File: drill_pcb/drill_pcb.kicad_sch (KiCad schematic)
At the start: 2 parts

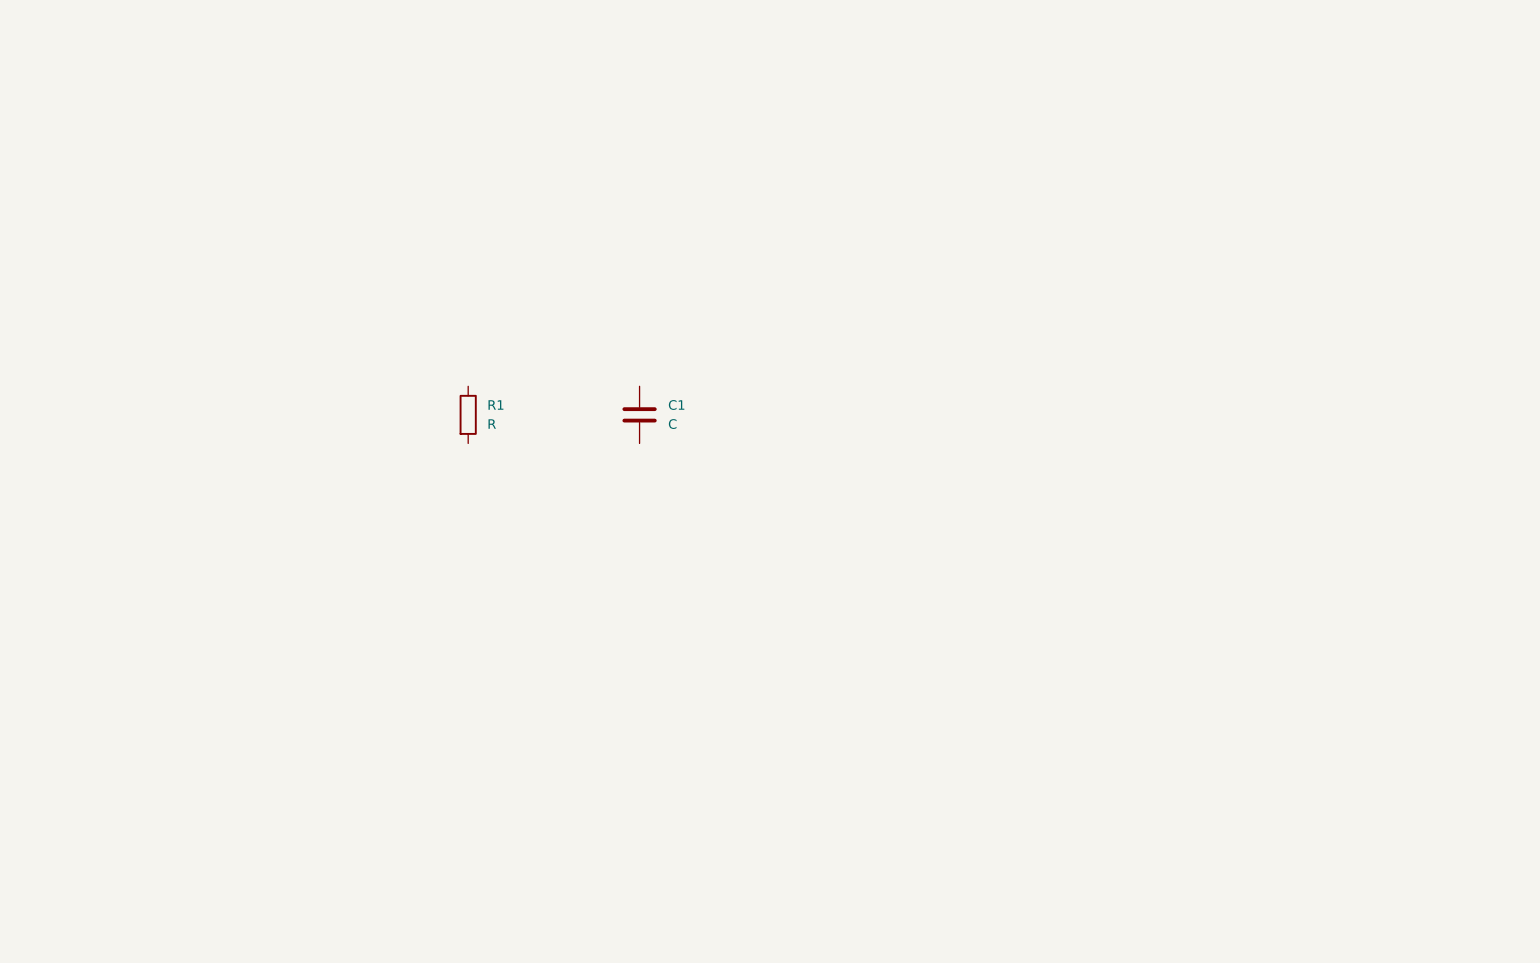
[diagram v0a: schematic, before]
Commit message: fix ERC errors
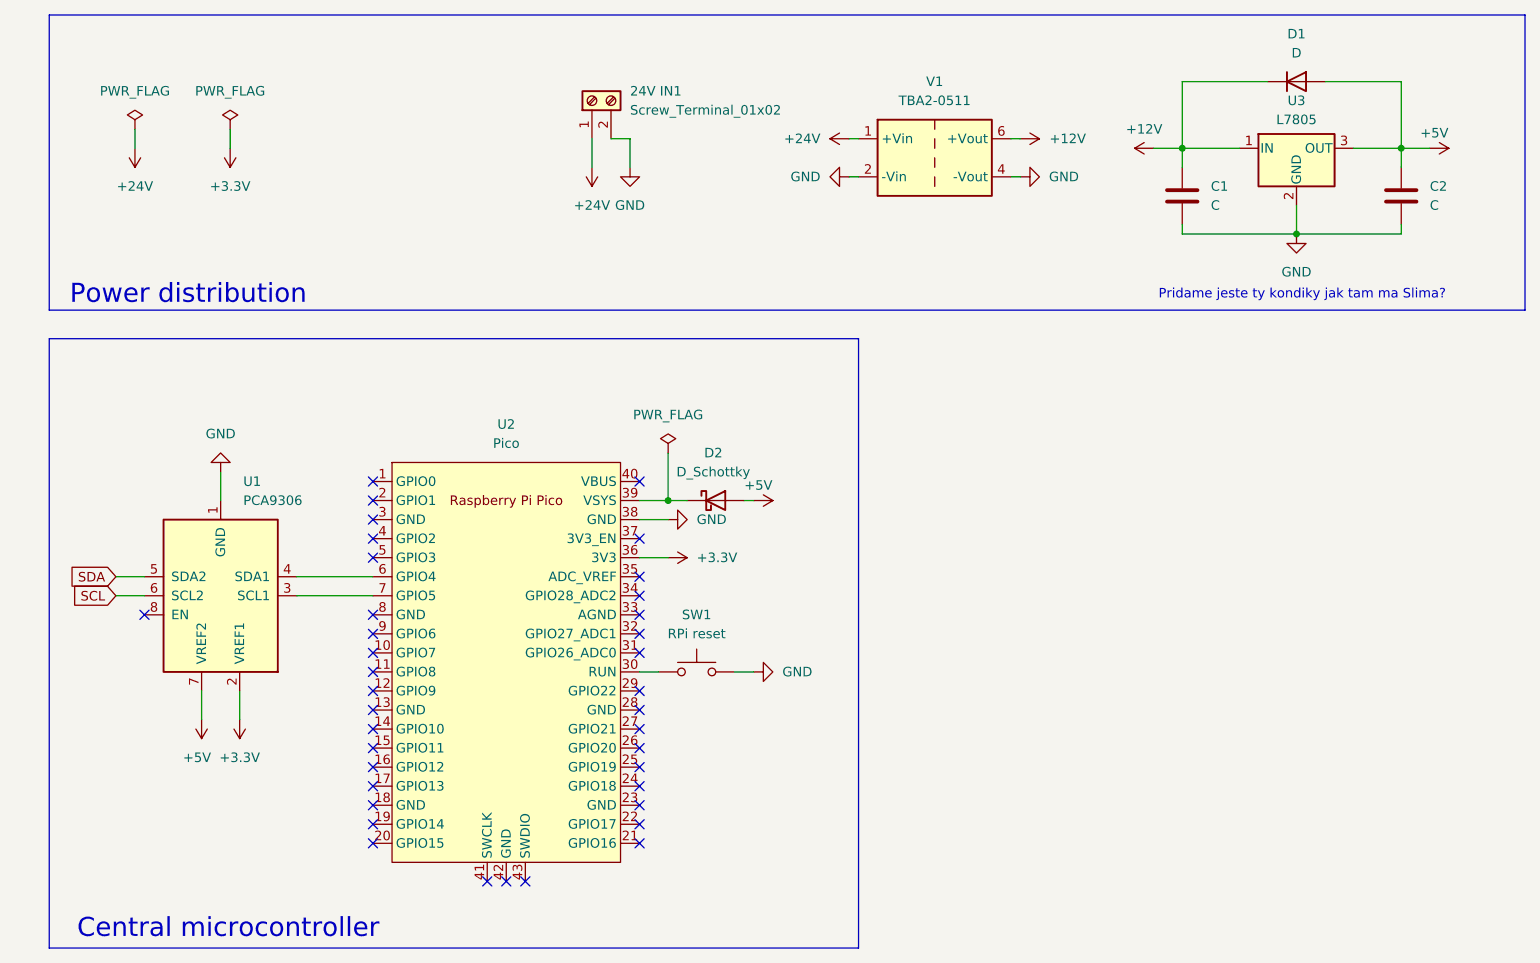
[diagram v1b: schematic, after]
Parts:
- removed R1: R, symbol Device:R
- added 24V IN1: Screw_Terminal_01x02, Connectors:DEANS, symbol Connector:Screw_Terminal_01x02
- added C2: C, Capacitor_SMD:C_1206_3216Metric_Pad1.33x1.80mm_HandSolder, symbol Device:C
- added D1: D, Diode_THT:D_DO-41_SOD81_P7.62mm_Horizontal, symbol Device:D
- added D2: D_Schottky, Diode_SMD:D_SOD-123, symbol Device:D_Schottky
- added SW1: RPi reset, Button_Switch_THT:SW_PUSH_6mm_H5mm, symbol Switch:SW_Push
- added U1: PCA9306, i2c_levl:i2c_levl_shifter, symbol Interface:PCA9306
- added U2: Pico, MCU_RaspberryPi_and_Boards:RPi_Pico_SMD_TH, symbol MCU_RaspberryPi_and_Boards:Pico
- added U3: L7805, Package_TO_SOT_THT:TO-220-3_Vertical, symbol Regulator_Linear:L7805
- added V1: TBA2-0511, i2c_levl:dcdc_menic, symbol Converter_DCDC:TBA2-0511
- C1: footprint (none) -> Capacitor_SMD:C_1206_3216Metric_Pad1.33x1.80mm_HandSolder
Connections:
- net +12V: now reaches C1.1
- net +12V: now also D1.1 (K), U3.1 (IN), V1.6 (+Vout)
- net GND: now reaches C1.2
- net GND: now also 24V IN1.2 (Pin_2), C2.2, SW1.2, U1.1 (GND), U2.38 (GND), U3.2 (GND), V1.2 (-Vin), V1.4 (-Vout)
- new net: D2.1 (K), U2.39 (VSYS)
- new net: SW1.1, U2.30 (RUN)
- new net: U1.4 (SDA1), U2.6 (GPIO4)
- new net: U1.3 (SCL1), U2.7 (GPIO5)
- new net +24V: 24V IN1.1 (Pin_1), V1.1 (+Vin)
- new net +3.3V: U1.2 (VREF1), U2.36 (3V3)
- new net +5V: C2.1, D1.2 (A), D2.2 (A), U1.7 (VREF2), U3.3 (OUT)
- new net SCL: U1.6 (SCL2)
- new net SDA: U1.5 (SDA2)
- no-connect marks 0 -> 38
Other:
- note added: "Central microcontroller"
- note added: "Power distribution"
- note added: "Pridame jeste ty kondiky jak tam ma Slima?"

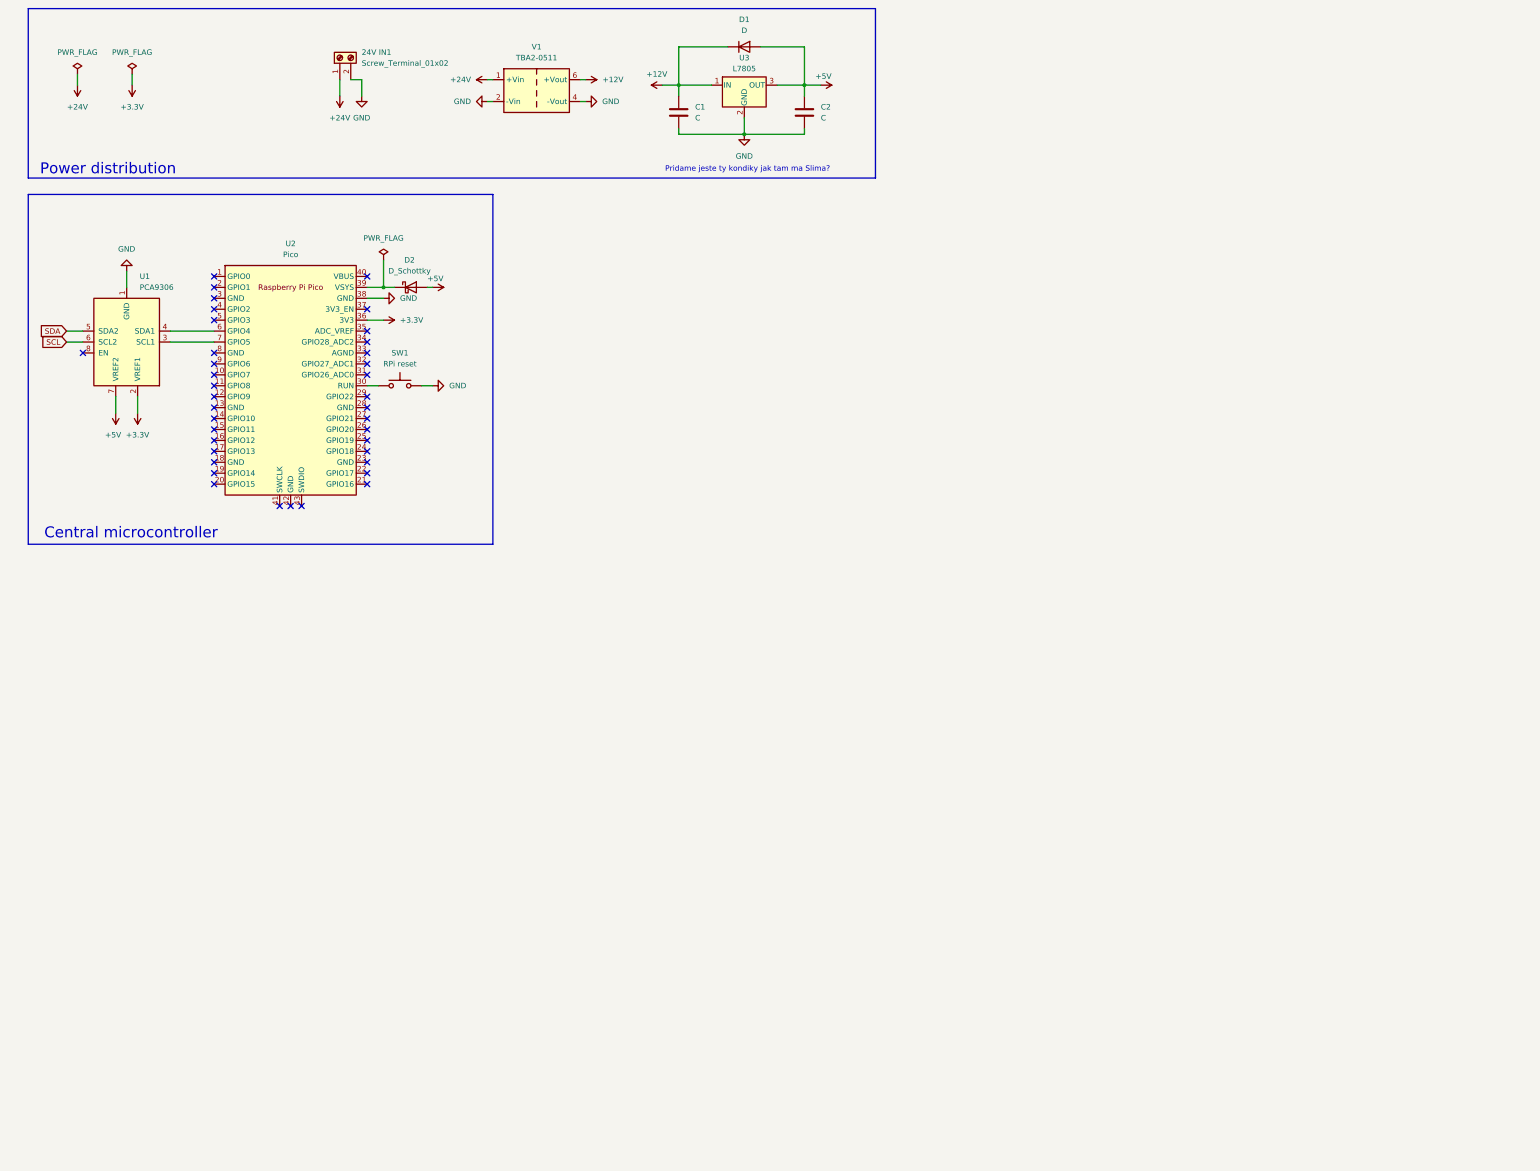
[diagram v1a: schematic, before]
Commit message: Rozsireni schématu o rizeni motoru. Ignorovani kicad backupu. Zavedeni kicad projektovych knihoven.
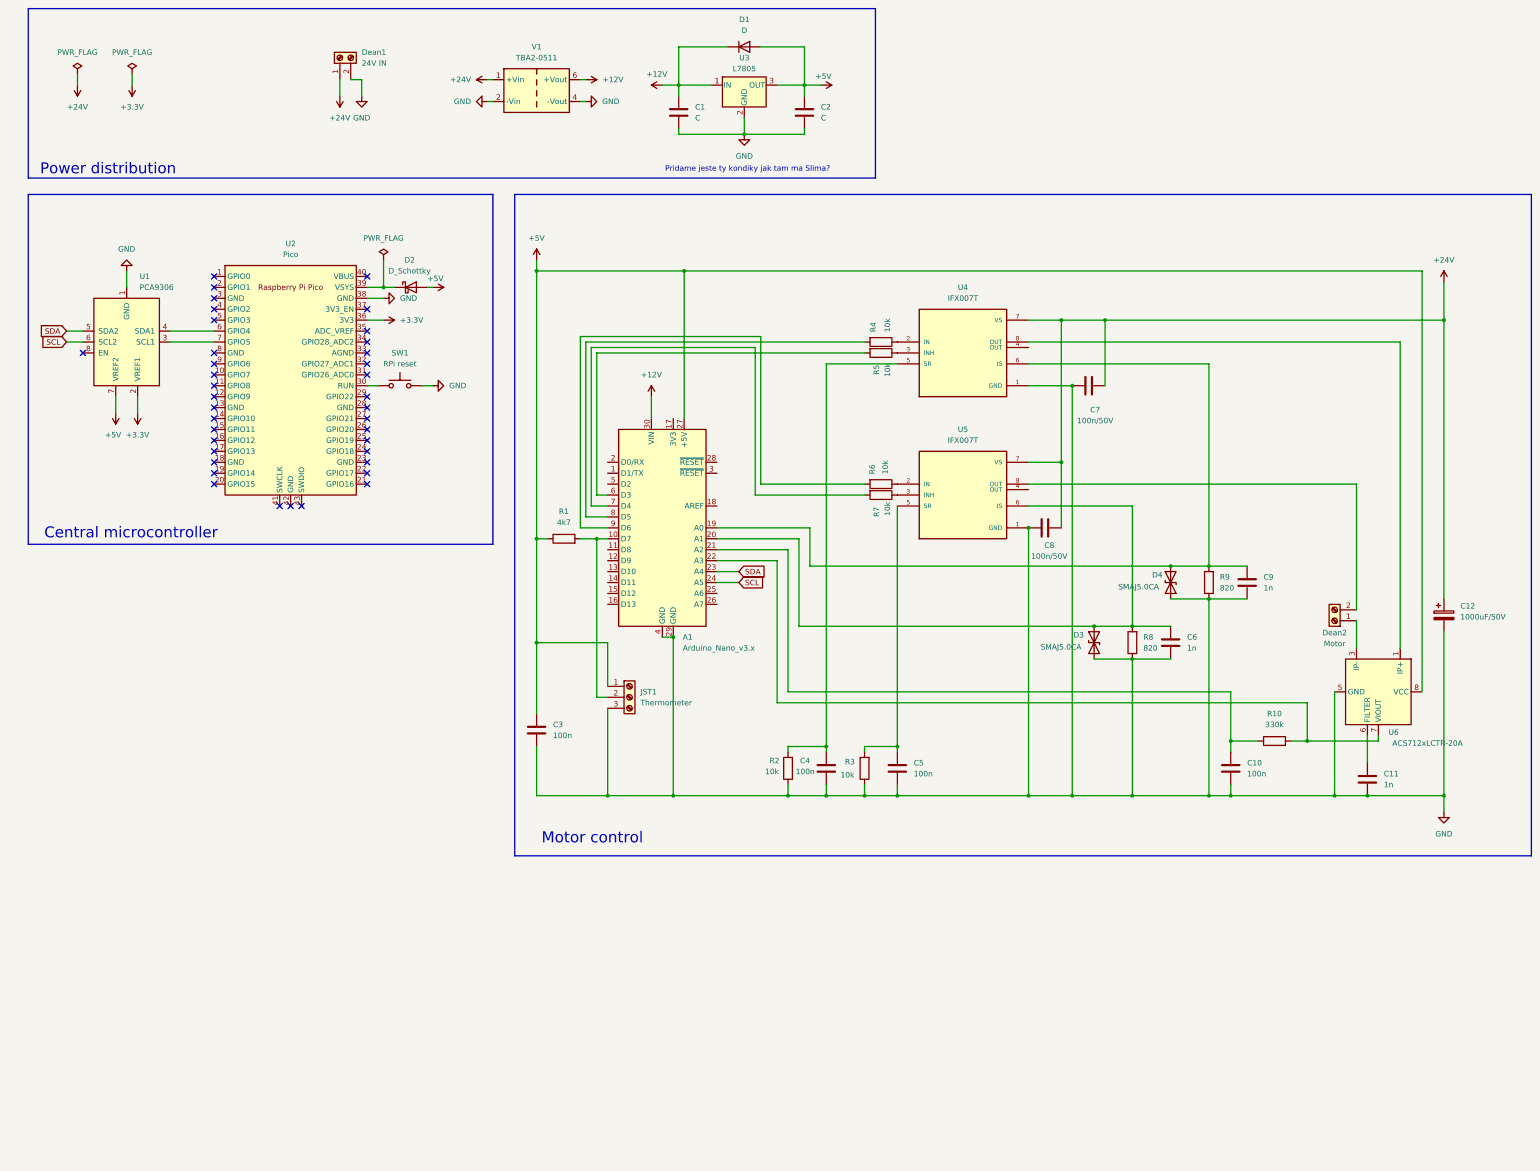
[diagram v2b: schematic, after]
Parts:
- added A1: Arduino_Nano_v3.x, Module:Arduino_Nano, symbol MCU_Module:Arduino_Nano_v3.x
- added C10, C3, C4, C5: 100n, Capacitor_SMD:C_1206_3216Metric_Pad1.33x1.80mm_HandSolder, symbol Device:C
- added C11, C6, C9: 1n, Capacitor_SMD:C_1206_3216Metric_Pad1.33x1.80mm_HandSolder, symbol Device:C
- added C12: 1000uF/50V, Capacitor_THT:CP_Radial_D12.5mm_P5.00mm, symbol Device:C_Polarized
- added C7, C8: 100n/50V, Capacitor_SMD:C_1206_3216Metric_Pad1.33x1.80mm_HandSolder, symbol Device:C
- added D3, D4: SMAJ5.0CA, Diode_SMD:D_SMA, symbol Diode:SMAJ5.0CA
- added Dean2: Motor, drill_T-DEAN:DEANS, symbol Connector:Screw_Terminal_01x02
- added JST1: Thermometer, Connector_JST:JST_XH_B3B-XH-A_1x03_P2.50mm_Vertical, symbol Connector:Screw_Terminal_01x03
- added R1: 4k7, Resistor_SMD:R_1206_3216Metric_Pad1.30x1.75mm_HandSolder, symbol Device:R
- added R10: 330k, Resistor_SMD:R_1206_3216Metric_Pad1.30x1.75mm_HandSolder, symbol Device:R
- added R2, R3, R4, R5, R6, R7: 10k, Resistor_SMD:R_1206_3216Metric_Pad1.30x1.75mm_HandSolder, symbol Device:R
- added R8, R9: 820, Resistor_SMD:R_1206_3216Metric_Pad1.30x1.75mm_HandSolder, symbol Device:R
- added U4, U5: IFX007T, drill_IFX007T:TO127P1500X440-8N_plusVias, symbol drill_IFX007T:IFX007T_uprava
- added U6: ACS712xLCTR-20A, Package_SO:SOIC-8_3.9x4.9mm_P1.27mm, symbol Sensor_Current:ACS712xLCTR-20A
- Dean1: renamed from 24V IN1; value Screw_Terminal_01x02 -> 24V IN; footprint Connectors:DEANS -> drill_T-DEAN:DEANS
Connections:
- net +12V: now also A1.30 (VIN)
- net +24V: now also C12.1, C7.2, C8.2, U4.7 (VS), U5.7 (VS)
- net +5V: now also A1.27 (+5V), C3.1, JST1.1 (Pin_1), R1.1, U6.8 (VCC)
- net GND: now also A1.29 (GND), A1.4 (GND), C10.2, C11.2, C12.2, C3.2, C4.2, C5.2, C6.2, C7.1, C8.1, C9.2, D3.1 (A1), D4.1 (A1), JST1.3 (Pin_3), R2.1, R3.1, R8.1, R9.1, U4.1 (GND), U5.1 (GND), U6.5 (GND)
- net SCL: now also A1.24 (A5)
- net SDA: now also A1.23 (A4)
- new net: R4.1, U4.2 (IN)
- new net: R5.1, U4.3 (INH)
- new net: C4.1, R2.2, U4.5 (SR)
- new net: A1.19 (A0), C9.1, D4.2 (A2), R9.2, U4.6 (IS)
- new net: U4.8 (OUT), U6.1 (IP+), U6.2 (IP+)
- new net: R6.1, U5.2 (IN)
- new net: R7.1, U5.3 (INH)
- new net: C5.1, R3.2, U5.5 (SR)
- new net: A1.20 (A1), C6.1, D3.2 (A2), R8.2, U5.6 (IS)
- new net: Dean2.2 (Pin_2), U5.8 (OUT)
- new net: C11.1, U6.6 (FILTER)
- new net: A1.21 (A2), C10.1, R10.1
- new net: A1.22 (A3), R10.2, U6.7 (VIOUT)
- new net: Dean2.1 (Pin_1), U6.3 (IP-), U6.4 (IP-)
- new net: A1.9 (D6), R6.2
- new net: A1.10 (D7), JST1.2 (Pin_2), R1.2
- new net: A1.6 (D3), R5.2
- new net: A1.7 (D4), R7.2
- new net: A1.8 (D5), R4.2
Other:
- note added: "Motor control"

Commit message: Library manager update
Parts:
- U1: footprint i2c_levl:i2c_levl_shifter -> drill_i2c_level_shifter:i2c_levl_shifter
- U2: footprint MCU_RaspberryPi_and_Boards:RPi_Pico_SMD_TH -> drill_RP-Pico Libraries:RPi_Pico_SMD_TH
- V1: footprint i2c_levl:dcdc_menic -> drill_dcdc_converter_LM2596:dcdc_menic
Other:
- moved on the sheet: A1, C1, C10, C11, C12, C2, C3, C4, C5, C6, C7, C8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
